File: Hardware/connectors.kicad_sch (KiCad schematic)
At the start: 47 parts, among them J10 4in1 ESC, J11 FPV, J12 GPS, J13 VTX, J14 RC Receiver, J9 ST_LINK

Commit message: Added Necessary Connectors, pads and comments in the respective file
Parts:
- removed TP42, TP46, TP50, TP56, TP58, TP64, TP72, TP82: GND, Solderpoint:Solderpad, symbol Connector:TestPoint
- removed TP44, TP52: 3.3V, Solderpoint:Solderpad, symbol Connector:TestPoint
- removed TP45, TP49, TP53, TP77: 5V, Solderpoint:Solderpad, symbol Connector:TestPoint
- removed TP61: 9V/12V, Solderpoint:Solderpad, symbol Connector:TestPoint
- removed TP62, TP67: GND, Solderpoint:BAT pad, symbol Connector:TestPoint
- removed TP65, TP74: VIDEO_OUT, Solderpoint:Solderpad, symbol Connector:TestPoint
- removed TP69, TP73, TP75, TP78: GPS, Solderpoint:Solderpad, symbol Connector:TestPoint
- removed TP70: VTX_TX, Solderpoint:Solderpad, symbol Connector:TestPoint
- removed TP81: PWR, Solderpoint:Solderpad, symbol Connector:TestPoint
- added J5: DJI, Connector_JST:JST_SH_SM06B-SRSS-TB_1x06-1MP_P1.00mm_Horizontal, symbol Connector_Generic:Conn_01x06
- added TP1, TP10, TP11, TP12, TP17, TP18, TP21, TP22, TP25, TP26, TP27, TP28, TP4, TP6: power, Solderpoint:Solderpad, symbol Connector:TestPoint
- added TP14, TP23: power, Solderpoint:BAT pad, symbol Connector:TestPoint
- renumbered J11 to J2, J9 to J3, J12 to J4, J10 to J6, J14 to J7, J13 to J8, TP48 to TP13, TP66 to TP15, TP54 to TP16, TP68 to TP19, TP43 to TP2, TP57 to TP20, TP60 to TP24, TP71 to TP29, TP47 to TP3, TP76 to TP30, TP79 to TP31, TP80 to TP32, TP51 to TP5, TP55 to TP7, TP59 to TP8, TP63 to TP9
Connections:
- net +3.3V: now also TP22.1, TP27.1
- net +5V: now also TP1.1, TP4.1
- net +pwr_out: now also J5.1 (Pin_1), TP11.1, TP6.1
- net GND: now also J5.2 (Pin_2), J5.5 (Pin_5), TP10.1, TP12.1, TP17.1, TP18.1, TP21.1, TP23.1, TP25.1, TP26.1, TP28.1
- net VBAT: now also TP14.1
- new net DJI_RX: J5.4 (Pin_4)
- new net DJI_SBUS: J5.6 (Pin_6)
- new net DJI_TX: J5.3 (Pin_3)
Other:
- note added: "(To Be Decided)"
- note added: "1) DJI support, Direct plug and play for DJI O3 Air Unit DJI FPV Air Unit v1 DJI FPV Vista / Caddx Vista DJI RunCam Link DJI Air Unit Lite (Vista variants)"
- note added: "2) JST connectors are either JST-SH 1mm or JST-GH 1.25mm industry standard"
- note added: "4 in 1 ESC"
- note added: "Analog FPV"
- note added: "Analog VTX"
- note added: "DJI Air Unit"
- note added: "GPS + Magnetometer module"
- note added: "RC Receiver (ELRS)"
- note added: "ST-Link Debugger"
- note added: "Servos"
- note removed: "Debugger"
- note removed: "FPV 9/12V"
- note removed: "GPS"
- note removed: "VTX"
- moved on the sheet: J2, J3, J4, J6, J7, J8, TP13, TP15, TP16, TP19, TP2, TP20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

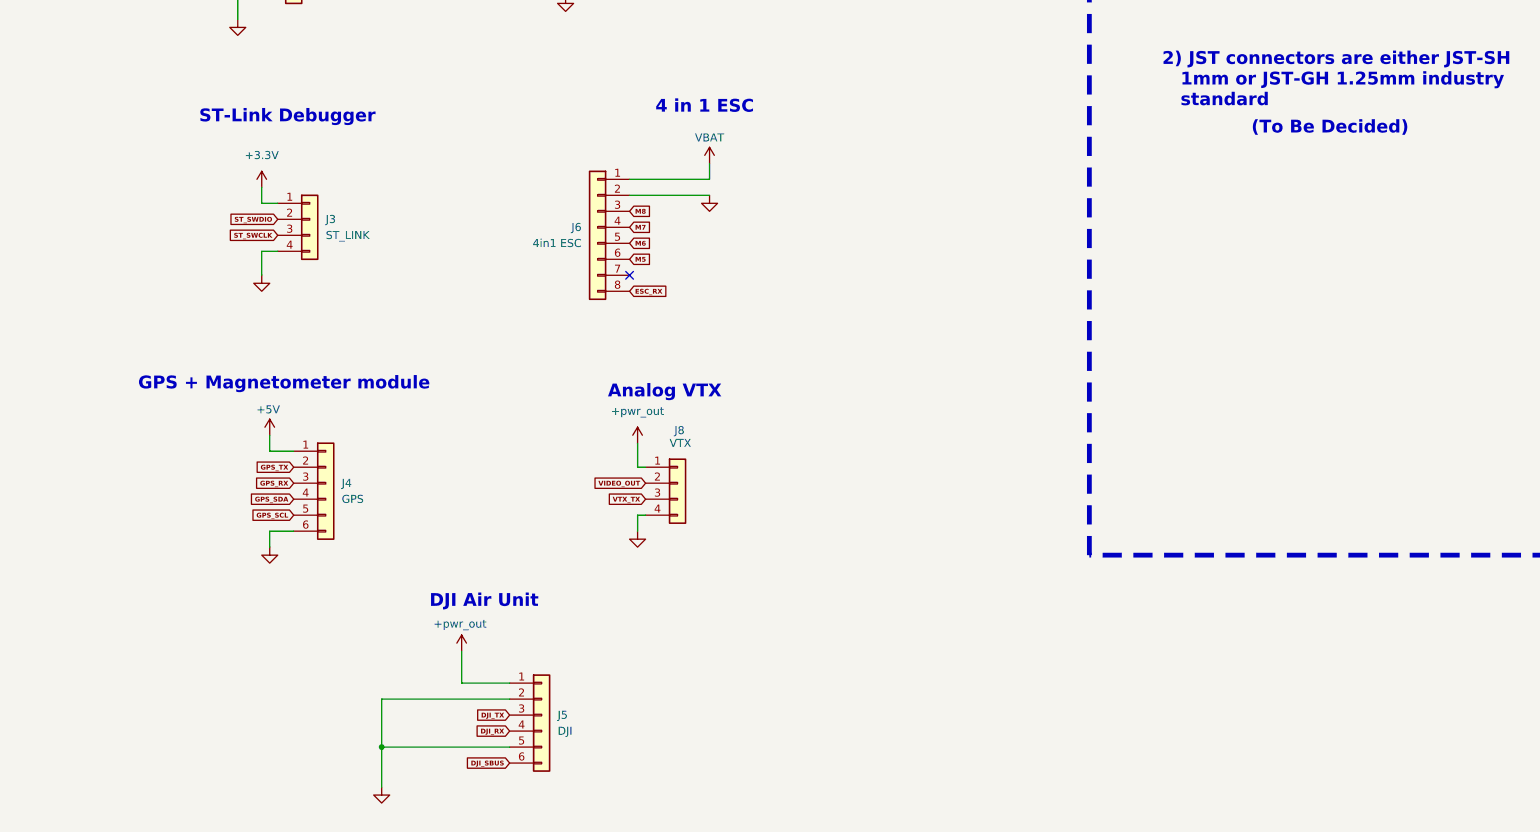
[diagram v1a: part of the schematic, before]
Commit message: Added Digital Airspeed Sensor Connector, Changed the Magnetometer
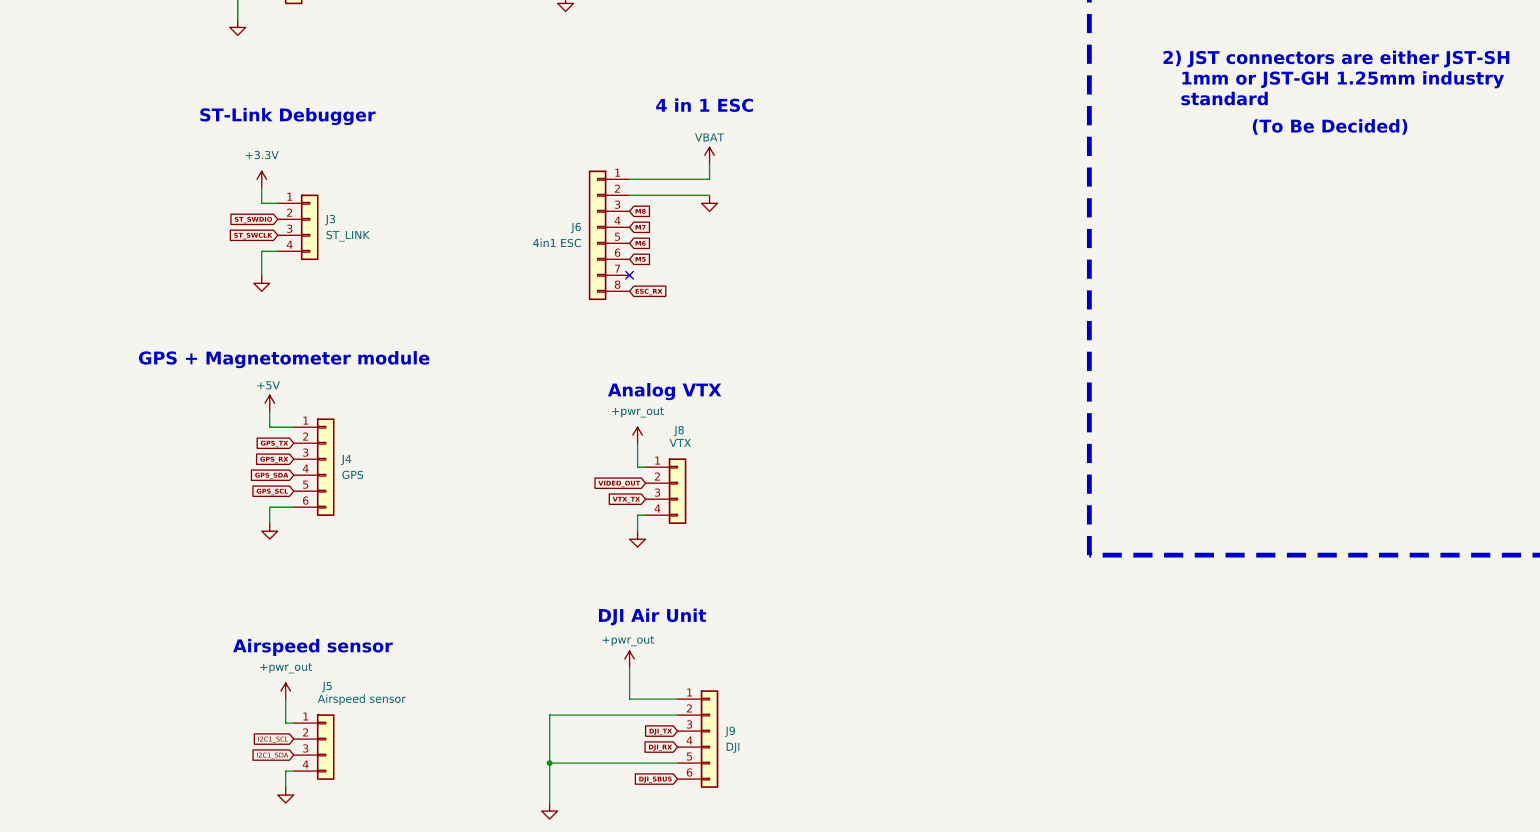
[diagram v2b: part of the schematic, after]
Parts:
- added J5: Airspeed sensor, memo:CONN-SMD_4P-P1.00_SM04B-SRSS-TB-LF-SN, symbol Connector_Generic:Conn_01x04
- renumbered J5 to J9
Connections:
- net +pwr_out: now also J5.1 (Pin_1)
- net GND: now also J5.4 (Pin_4)
- new net I2C1_SCL: J5.2 (Pin_2)
- new net I2C1_SDA: J5.3 (Pin_3)
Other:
- note added: "Airspeed sensor"
- moved on the sheet: J4, J9

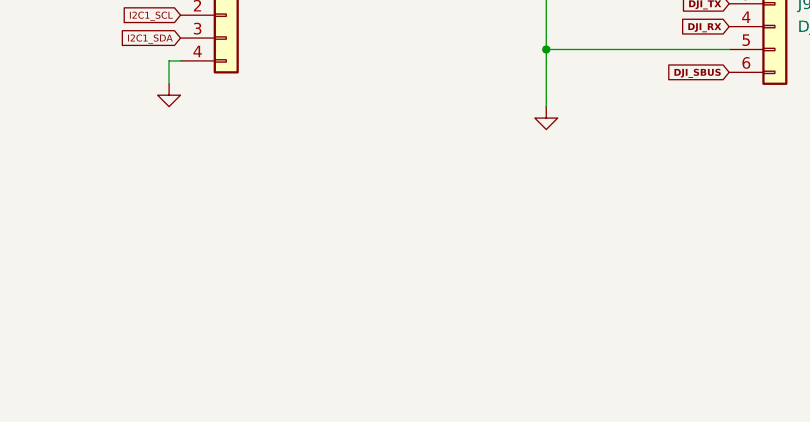
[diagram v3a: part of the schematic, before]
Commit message: added CAN connector
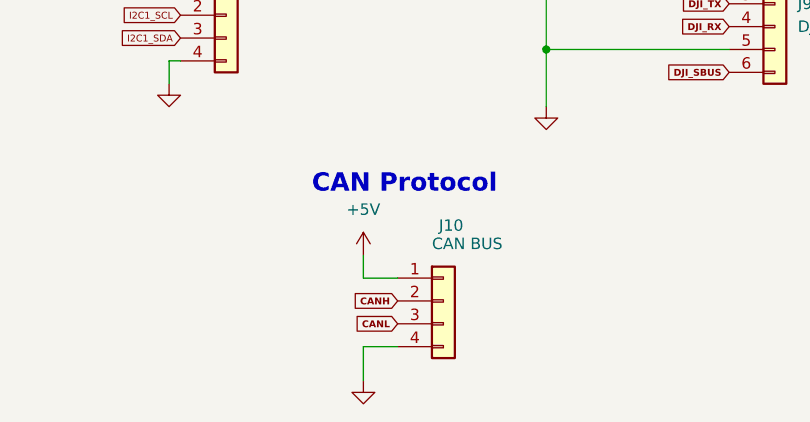
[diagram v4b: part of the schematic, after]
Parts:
- added J10: CAN BUS, memo:CONN-SMD_4P-P1.00_SM04B-SRSS-TB-LF-SN, symbol Connector_Generic:Conn_01x04
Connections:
- net +5V: now also J10.1 (Pin_1)
- net GND: now also J10.4 (Pin_4)
- new net CANH: J10.2 (Pin_2)
- new net CANL: J10.3 (Pin_3)
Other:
- note added: "CAN Protocol"

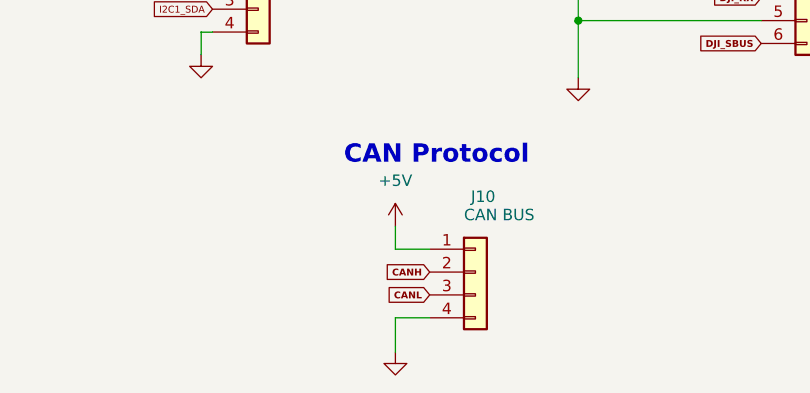
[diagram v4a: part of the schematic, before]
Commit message: added firmware drivers for all sensors for the test board
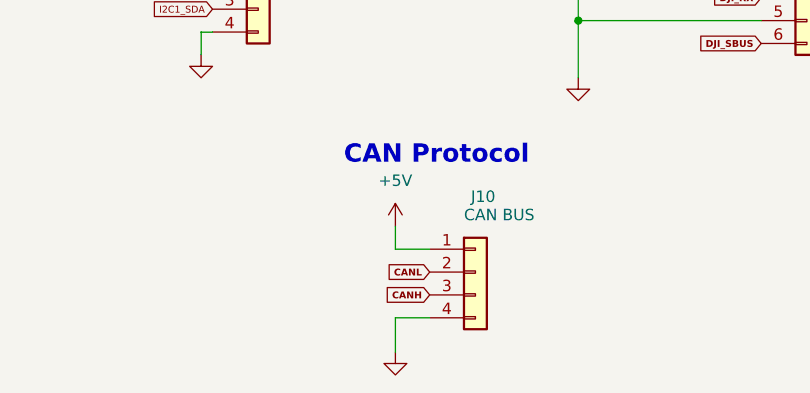
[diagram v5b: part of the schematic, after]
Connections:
- net CANH: now also J10.3 (Pin_3); no longer J10.2 (Pin_2)
- net CANL: now also J10.2 (Pin_2); no longer J10.3 (Pin_3)

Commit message: changed hella stuff in firmware plan and hardware pcb layout
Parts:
- added J11: CAN BUS, memo:CONN-SMD_4P-P1.00_SM04B-SRSS-TB-LF-SN, symbol Connector_Generic:Conn_01x04
- added TP33, TP34, TP35, TP36: power, Solderpoint:Solderpad, symbol Connector:TestPoint
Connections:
- net ESC_RX is gone; now on net M5: J6.8 (Pin_8)
- net +5V: now also J11.1 (Pin_1); no longer J2.1 (Pin_1)
- net +pwr_out: now also J2.1 (Pin_1)
- net GND: now also J11.4 (Pin_4)
- net GPS_SCL: now also TP35.1
- net GPS_SDA: now also TP36.1
- net M5: no longer J6.6 (Pin_6)
- net M6: now also J6.7 (Pin_7); no longer J6.5 (Pin_5)
- net M7: now also J6.6 (Pin_6); no longer J6.4 (Pin_4)
- net M8: now also J6.5 (Pin_5); no longer J6.3 (Pin_3)
- net VBAT: no longer TP14.1
- net VIDEO_OUT: now also TP34.1
- net VTX_TX: now also TP33.1
- new net +VABT: TP14.1
- new net CURR: J6.4 (Pin_4)
- new net EXPANSION_RX: J11.3 (Pin_3)
- new net EXPANSION_TX: J11.2 (Pin_2)
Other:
- note added: "EXPANSION BOARD"
- moved on the sheet: J10, J2, J3, J4, J5, J6, J7, J8, J9

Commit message: layout progress
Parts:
- added TP37, TP38: sensors, Solderpoint:Solderpad, symbol Connector:TestPoint
- TP33, TP34, TP35, TP36: value power -> sensors
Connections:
- net +3.3V: now also J10.1 (Pin_1)
- net +5V: no longer J10.1 (Pin_1)
- net CANH: now also TP38.1
- net CANL: now also TP37.1
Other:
- moved on the sheet: TP33, TP34, TP35, TP36

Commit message: hella shit configured, layout progress
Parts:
- added TP39, TP40, TP41, TP42: sensors, Solderpoint:Solderpad, symbol Connector:TestPoint
- added TP43, TP45: power, Solderpoint:Solderpad, symbol Connector:TestPoint
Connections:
- net VBAT is gone; now on net +VBAT: J6.1 (Pin_1)
- net +5V: now also J2.4 (Pin_4), J4.6 (Pin_6), TP43.1; no longer J4.1 (Pin_1), TP31.1
- net +pwr_out: no longer J2.1 (Pin_1)
- net EXPANSION_RX: now also J11.2 (Pin_2); no longer J11.3 (Pin_3)
- net EXPANSION_TX: now also J11.3 (Pin_3); no longer J11.2 (Pin_2)
- net GND: now also J2.1 (Pin_1), J4.1 (Pin_1), TP31.1, TP45.1; no longer J2.4 (Pin_4), J4.6 (Pin_6)
- net GPS_RX: now also TP36.1
- net GPS_SCL: no longer TP35.1
- net GPS_SDA: no longer TP36.1
- net GPS_TX: now also TP35.1
- net I2C1_SCL: now also TP41.1
- net I2C1_SDA: now also TP42.1
- net +VABT renamed +VBAT
- net CANH renamed CAN_P
- net CANL renamed CAN_N
- new net I2C2_SCL: TP39.1
- new net I2C2_SDA: TP40.1
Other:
- note added: "Extra Pads"
- moved on the sheet: J2, J4, TP33, TP34, TP35, TP36, TP37, TP38
